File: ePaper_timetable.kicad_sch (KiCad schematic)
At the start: 70 parts, among them J1 USB_C_Receptacle_USB2.0, J2 52435-2471, J3 Conn_01x03_Socket, J4 Charging input - 5V, J5 Conn_01x03_Socket, J6 Conn_01x03_Socket, J7 Conn_01x04_Socket, J8 Battery connector, J9 Conn_01x01_Pin, Q1 BSS138, Q2 AO3401A, Q3 FS8205A, Q4 BSS138, SW1 SW_Push, SW2 SW_Push, SW3 SW_Push, SW4 SW_Push, SW5 SW_Push, U1 USBLC6-2SC6, U2 DW01A, U3 TP4056

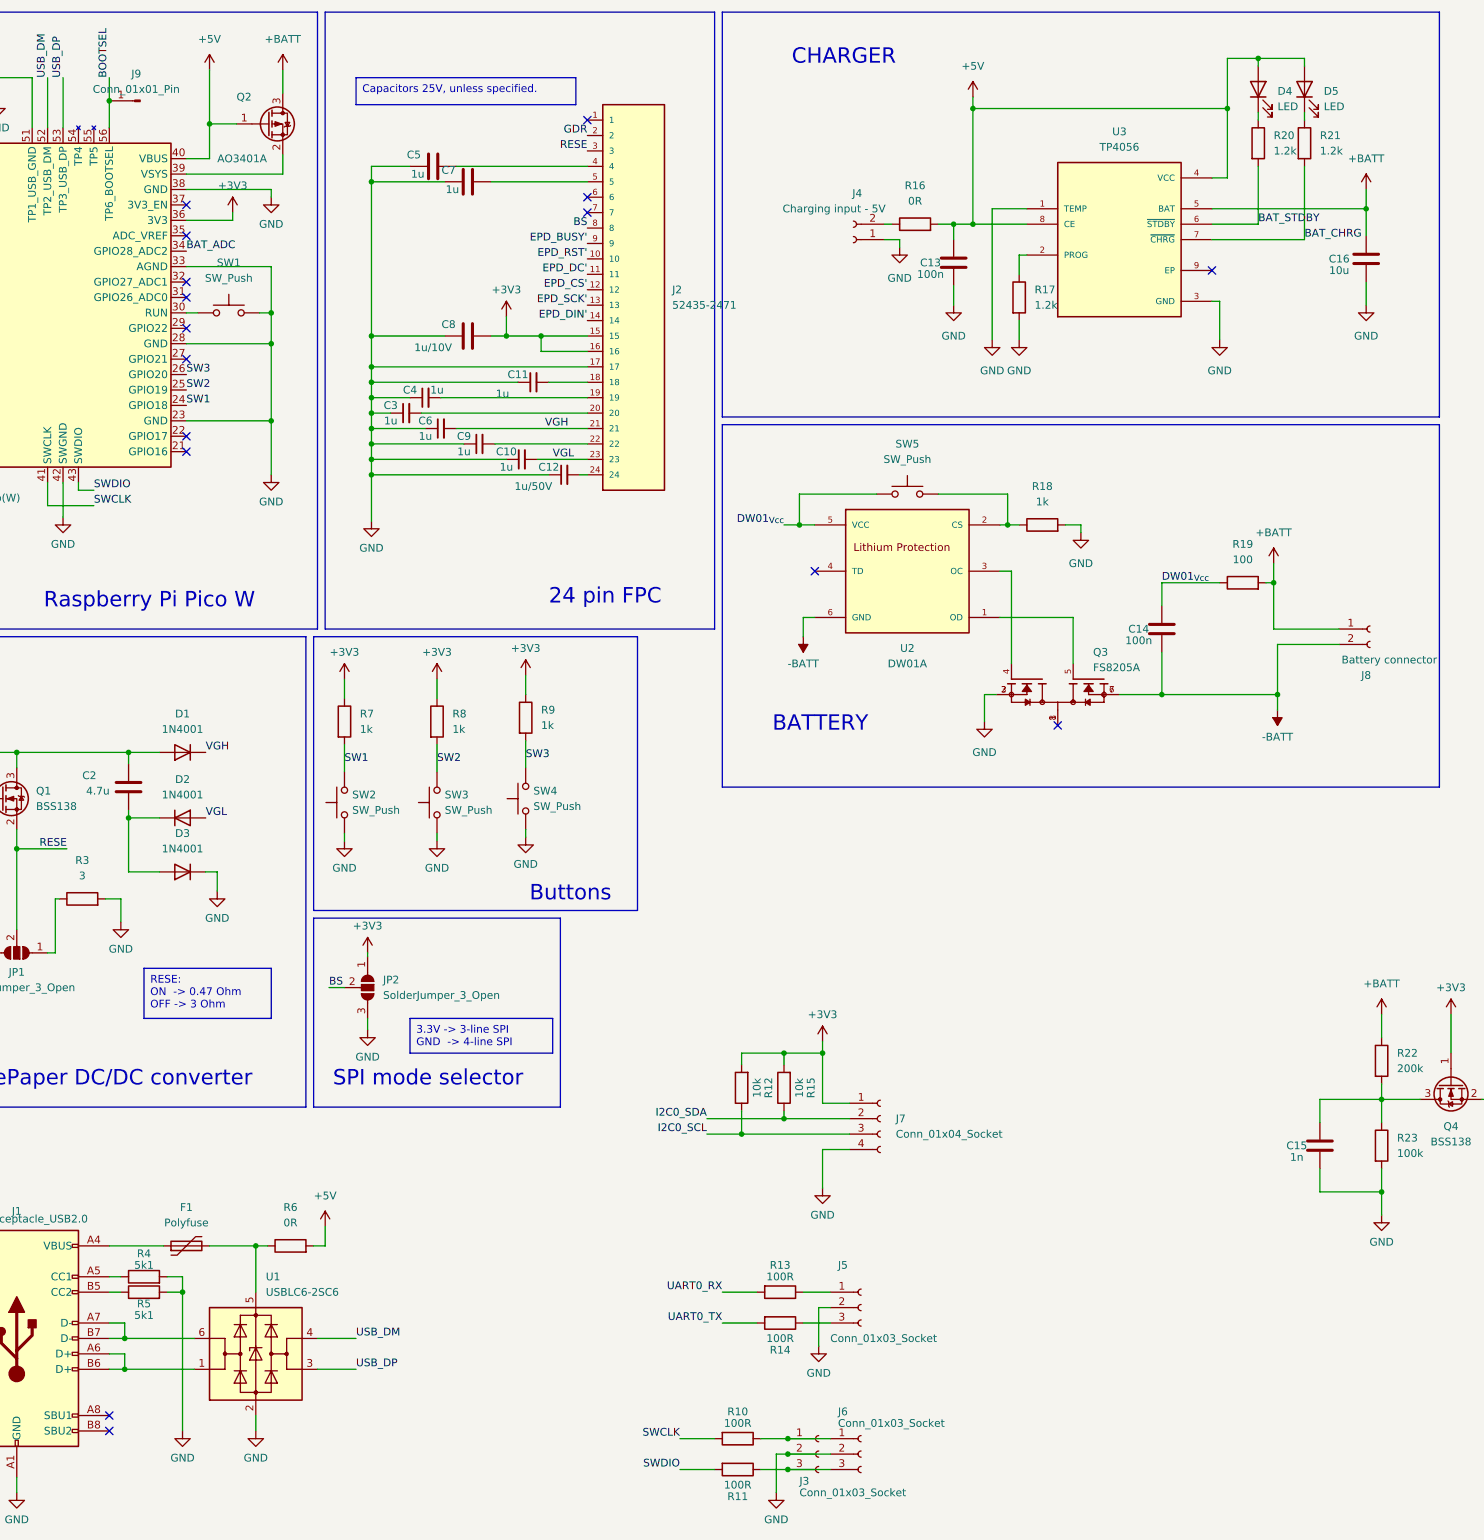
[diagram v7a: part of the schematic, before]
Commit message: fpc connector fix
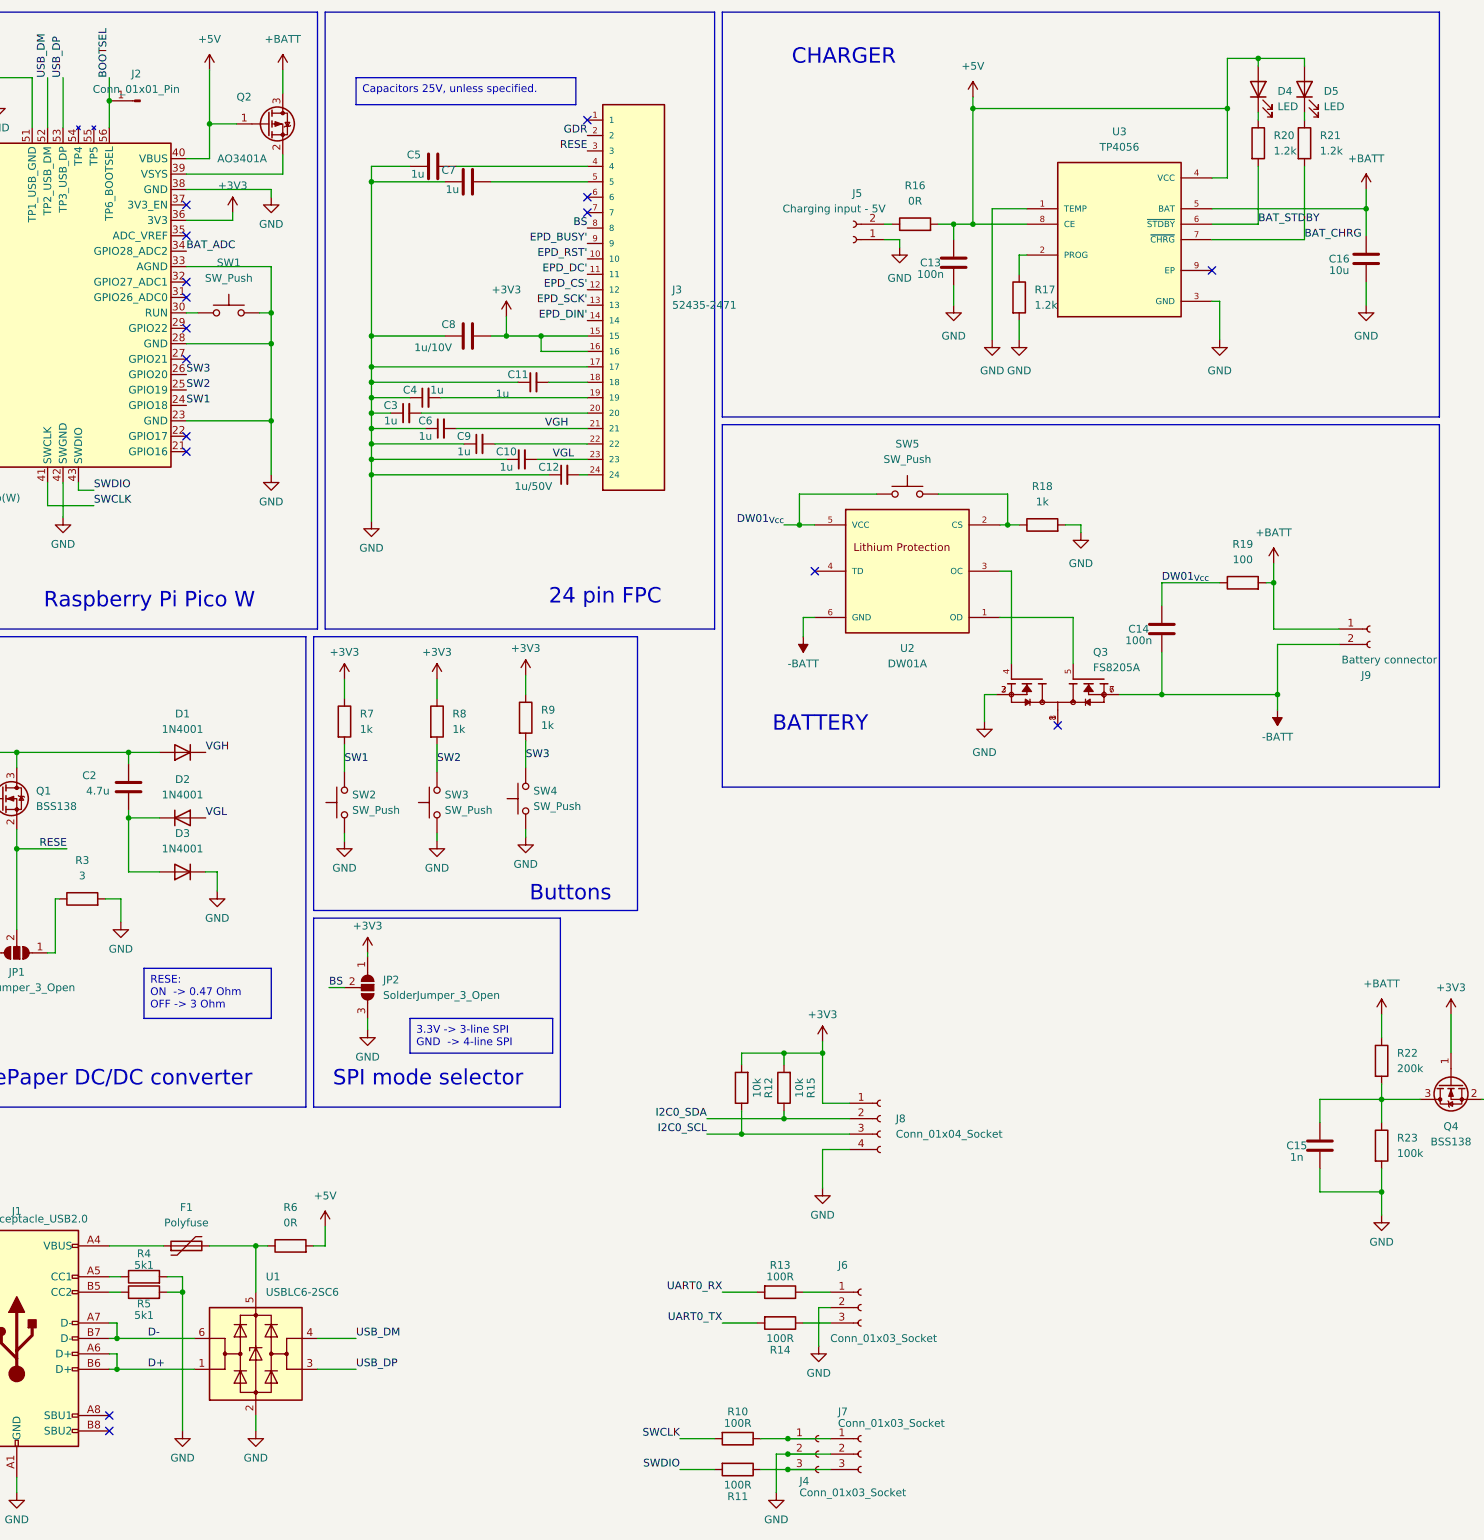
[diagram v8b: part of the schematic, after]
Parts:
- renumbered J9 to J2, J2 to J3, J3 to J4, J4 to J5, J5 to J6, J6 to J7, J7 to J8, J8 to J9
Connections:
- net D+: now reaches J1.A6 (D+), J1.B6 (D+), U1.1 (I/O1)
- net D-: now reaches J1.A7 (D-), J1.B7 (D-), U1.6 (I/O1)
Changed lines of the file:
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@@
   (junction (at 247.65 29.845) (diameter 0) (color 0 0 0 0)
   )
-  (junction (at 66.04 237.49) (diameter 0) (color 0 0 0 0)
-  )
   (junction (at 90.17 63.5) (diameter 0) (color 0 0 0 0)
   )
@@
   (junction (at 174.625 185.42) (diameter 0) (color 0 0 0 0)
   )
+  (junction (at 64.77 232.41) (diameter 0) (color 0 0 0 0)
+  )
   (junction (at 106.68 90.17) (diameter 0) (color 0 0 0 0)
   )
@@
   (junction (at 134.62 67.31) (diameter 0) (color 0 0 0 0)
   )
+  (junction (at 64.77 237.49) (diameter 0) (color 0 0 0 0)
+  )
   (junction (at 174.625 196.215) (diameter 0) (color 0 0 0 0)
   )
   (junction (at 48.26 151.765) (diameter 0) (color 0 0 0 0)
   )
-  (junction (at 66.04 232.41) (diameter 0) (color 0 0 0 0)
-  )
   (junction (at 106.68 82.55) (diameter 0) (color 0 0 0 0)
   )
@@
     (stroke (width 0) (type default))
   )
-  (wire (pts (xy 66.04 232.41) (xy 77.47 232.41))
+  (wire (pts (xy 63.5 232.41) (xy 64.77 232.41))
     (stroke (width 0) (type default))
   )
@@
     (stroke (width 0) (type default))
   )
-  (wire (pts (xy 66.04 237.49) (xy 66.04 234.95))
-    (stroke (width 0) (type default))
-  )
   (wire (pts (xy 247.65 29.845) (xy 205.74 29.845))
     (stroke (width 0) (type default))
@@
     (stroke (width 0) (type default))
   )
-  (wire (pts (xy 63.5 234.95) (xy 66.04 234.95))
-    (stroke (width 0) (type default))
-  )
   (wire (pts (xy 167.64 198.755) (xy 185.42 198.755))
     (stroke (width 0) (type default))
@@
     (stroke (width 0) (type default))
   )
-  (wire (pts (xy 63.5 229.87) (xy 66.04 229.87))
+  (wire (pts (xy 92.075 40.64) (xy 92.075 37.465))
     (stroke (width 0) (type default))
   )
-  (wire (pts (xy 92.075 40.64) (xy 92.075 37.465))
+  (wire (pts (xy 64.77 234.95) (xy 64.77 237.49))
     (stroke (width 0) (type default))
   )
@@
     (stroke (width 0) (type default))
   )
+  (wire (pts (xy 64.77 229.87) (xy 64.77 232.41))
+    (stroke (width 0) (type default))
+  )
   (wire (pts (xy 53.34 91.44) (xy 53.34 95.25))
     (stroke (width 0) (type default))
@@
     (stroke (width 0) (type default))
   )
-  (wire (pts (xy 66.04 232.41) (xy 66.04 229.87))
-    (stroke (width 0) (type default))
-  )
   (wire (pts (xy 106.68 87.63) (xy 106.68 85.09))
     (stroke (width 0) (type default))
@@
     (stroke (width 0) (type default))
   )
+  (wire (pts (xy 63.5 234.95) (xy 64.77 234.95))
+    (stroke (width 0) (type default))
+  )
   (wire (pts (xy 210.185 113.665) (xy 222.25 113.665))
     (stroke (width 0) (type default))
@@
     (stroke (width 0) (type default))
   )
-  (wire (pts (xy 66.04 237.49) (xy 77.47 237.49))
+  (wire (pts (xy 63.5 237.49) (xy 64.77 237.49))
     (stroke (width 0) (type default))
   )
@@
     (stroke (width 0) (type default))
   )
+  (wire (pts (xy 64.77 237.49) (xy 77.47 237.49))
+    (stroke (width 0) (type default))
+  )
   (wire (pts (xy 202.565 48.895) (xy 205.74 48.895))
     (stroke (width 0) (type default))
@@
     (stroke (width 0) (type default))
   )
+  (wire (pts (xy 64.77 232.41) (xy 77.47 232.41))
+    (stroke (width 0) (type default))
+  )
   (wire (pts (xy 252.73 48.895) (xy 252.73 39.37))
     (stroke (width 0) (type default))
@@
     (stroke (width 0) (type default))
   )
+  (wire (pts (xy 63.5 229.87) (xy 64.77 229.87))
+    (stroke (width 0) (type default))
+  )
   (wire (pts (xy 128.905 64.135) (xy 128.905 67.31))
     (stroke (width 0) (type default))
@@
     (stroke (width 0) (type default))
   )
-  (wire (pts (xy 63.5 232.41) (xy 66.04 232.41))
-    (stroke (width 0) (type default))
-  )
   (wire (pts (xy 255.27 115.57) (xy 266.065 115.57))
     (stroke (width 0) (type default))
@@
     (stroke (width 0) (type default))
   )
-  (wire (pts (xy 63.5 237.49) (xy 66.04 237.49))
-    (stroke (width 0) (type default))
-  )
   (wire (pts (xy 24.765 153.035) (xy 24.765 160.655))
     (stroke (width 0) (type default))
@@
     (effects (font (size 1.27 1.27)) (justify right bottom))
   )
+  (label "D+" (at 69.85 237.49 0) (fields_autoplaced)
+    (effects (font (size 1.27 1.27)) (justify left bottom))
+  )
   (label "I2C0_SDA" (at 35.56 50.8 180) (fields_autoplaced)
     (effects (font (size 1.27 1.27)) (justify right bottom))
@@
     (effects (font (size 1.27 1.27)) (justify right bottom))
   )
+  (label "D-" (at 69.85 232.41 0) (fields_autoplaced)
+    (effects (font (size 1.27 1.27)) (justify left bottom))
+  )
   (label "VGH" (at 79.375 135.89 0) (fields_autoplaced)
     (effects (font (size 1.27 1.27)) (justify left bottom))
@@
   (symbol (lib_id "Connector:Conn_01x02_Socket") (at 186.055 51.435 180) (unit 1)
     (in_bom yes) (on_board yes) (dnp no)
-    (property "Reference" "J4" (at 186.69 43.815 0)
+    (property "Reference" "J5" (at 186.69 43.815 0)
       (effects (font (size 1.27 1.27)))
     )
@@
       (project "ePaper_timetable"
         (path "/4d14e74c-b765-48d8-b3f5-8cedb4042594"
-          (reference "J4") (unit 1)
+          (reference "J5") (unit 1)
         )
       )
@@
   (symbol (lib_id "Connector:Conn_01x02_Socket") (at 271.145 115.57 0) (unit 1)
     (in_bom yes) (on_board yes) (dnp no)
-    (property "Reference" "J8" (at 270.51 123.19 0)
+    (property "Reference" "J9" (at 270.51 123.19 0)
       (effects (font (size 1.27 1.27)))
     )
@@
       (project "ePaper_timetable"
         (path "/4d14e74c-b765-48d8-b3f5-8cedb4042594"
-          (reference "J8") (unit 1)
+          (reference "J9") (unit 1)
         )
       )
@@
   (symbol (lib_id "52435-2471:52435-2471") (at 149.86 59.69 0) (unit 1)
     (in_bom yes) (on_board yes) (dnp no) (fields_autoplaced)
-    (property "Reference" "J2" (at 156.21 59.69 0)
+    (property "Reference" "J3" (at 156.21 59.69 0)
       (effects (font (size 1.27 1.27)) (justify left))
     )
@@
       (project "ePaper_timetable"
         (path "/4d14e74c-b765-48d8-b3f5-8cedb4042594"
-          (reference "J2") (unit 1)
+          (reference "J3") (unit 1)
         )
       )
@@
   (symbol (lib_id "Connector:Conn_01x03_Socket") (at 187.325 251.46 0) (unit 1)
     (in_bom yes) (on_board yes) (dnp no)
-    (property "Reference" "J6" (at 183.515 244.475 0)
+    (property "Reference" "J7" (at 183.515 244.475 0)
       (effects (font (size 1.27 1.27)) (justify left))
     )
@@
       (project "ePaper_timetable"
         (path "/4d14e74c-b765-48d8-b3f5-8cedb4042594"
-          (reference "J6") (unit 1)
+          (reference "J7") (unit 1)
         )
       )
@@
   (symbol (lib_id "Connector:Conn_01x03_Socket") (at 187.325 227.33 0) (unit 1)
     (in_bom yes) (on_board yes) (dnp no)
-    (property "Reference" "J5" (at 183.515 220.345 0)
+    (property "Reference" "J6" (at 183.515 220.345 0)
       (effects (font (size 1.27 1.27)) (justify left))
     )
@@
       (project "ePaper_timetable"
         (path "/4d14e74c-b765-48d8-b3f5-8cedb4042594"
-          (reference "J5") (unit 1)
+          (reference "J6") (unit 1)
         )
       )
@@
   (symbol (lib_id "Connector:Conn_01x01_Pin") (at 68.58 28.575 180) (unit 1)
     (in_bom yes) (on_board yes) (dnp no) (fields_autoplaced)
-    (property "Reference" "J9" (at 67.945 24.13 0)
+    (property "Reference" "J2" (at 67.945 24.13 0)
       (effects (font (size 1.27 1.27)))
     )
@@
       (project "ePaper_timetable"
         (path "/4d14e74c-b765-48d8-b3f5-8cedb4042594"
-          (reference "J9") (unit 1)
+          (reference "J2") (unit 1)
         )
       )
@@
   (symbol (lib_id "Connector:Conn_01x04_Socket") (at 190.5 196.215 0) (unit 1)
     (in_bom yes) (on_board yes) (dnp no) (fields_autoplaced)
-    (property "Reference" "J7" (at 193.04 196.215 0)
+    (property "Reference" "J8" (at 193.04 196.215 0)
       (effects (font (size 1.27 1.27)) (justify left))
     )
@@
       (project "ePaper_timetable"
         (path "/4d14e74c-b765-48d8-b3f5-8cedb4042594"
-          (reference "J7") (unit 1)
+          (reference "J8") (unit 1)
         )
       )
@@
   (symbol (lib_id "Connector:Conn_01x03_Socket") (at 180.34 251.46 0) (unit 1)
     (in_bom yes) (on_board yes) (dnp no)
-    (property "Reference" "J3" (at 177.165 255.905 0)
+    (property "Reference" "J4" (at 177.165 255.905 0)
       (effects (font (size 1.27 1.27)) (justify left))
     )
@@
       (project "ePaper_timetable"
         (path "/4d14e74c-b765-48d8-b3f5-8cedb4042594"
-          (reference "J3") (unit 1)
+          (reference "J4") (unit 1)
         )
       )
